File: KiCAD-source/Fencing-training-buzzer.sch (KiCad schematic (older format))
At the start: 13 parts, among them J1 Con, J2 DC Jack 5V, U1 74HC02

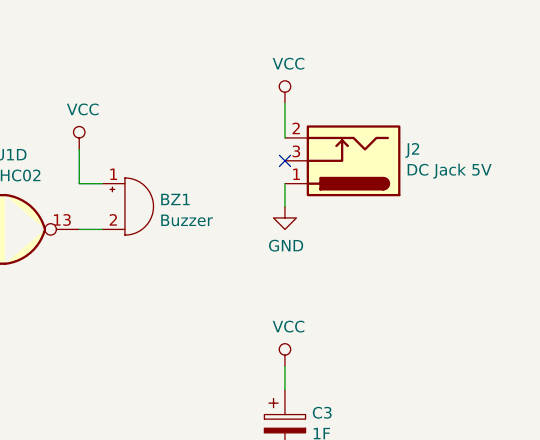
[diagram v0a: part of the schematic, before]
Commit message: Fix reverse polarity error at the barrel jack
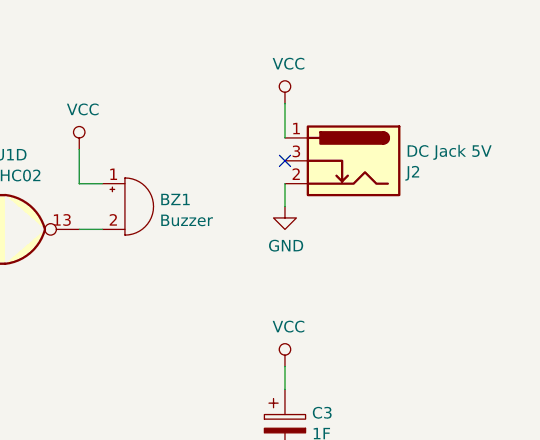
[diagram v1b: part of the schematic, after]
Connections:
- net GND: now also J2.2; no longer J2.1
- net VCC: now also J2.1; no longer J2.2
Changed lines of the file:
@@
 F 3 "~" H 8600 3360 50  0001 C CNN
 	1    8550 3400
-	-1   0    0    1
+	-1   0    0    -1
 $EndComp
 $Comp
